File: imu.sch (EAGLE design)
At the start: 51 parts, among them IC1 TM4C123[6,F]XXPM, IC2 FT230XQ, U1 MPU-6000QFN-24, U2 ADXL345

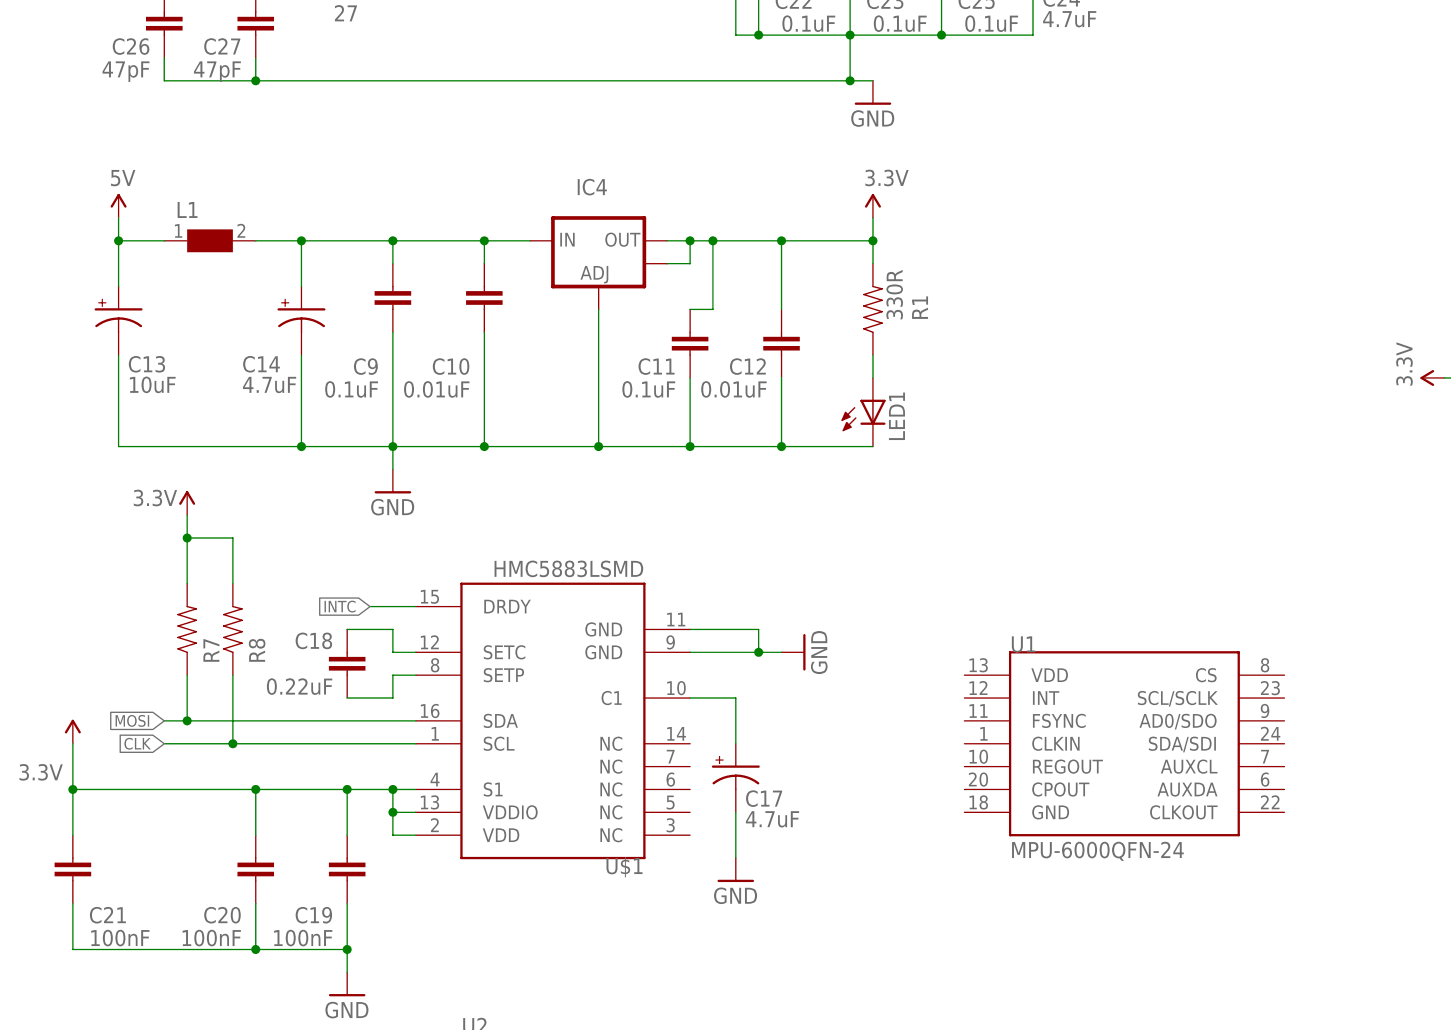
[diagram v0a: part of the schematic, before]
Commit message: Modification to schematics and board
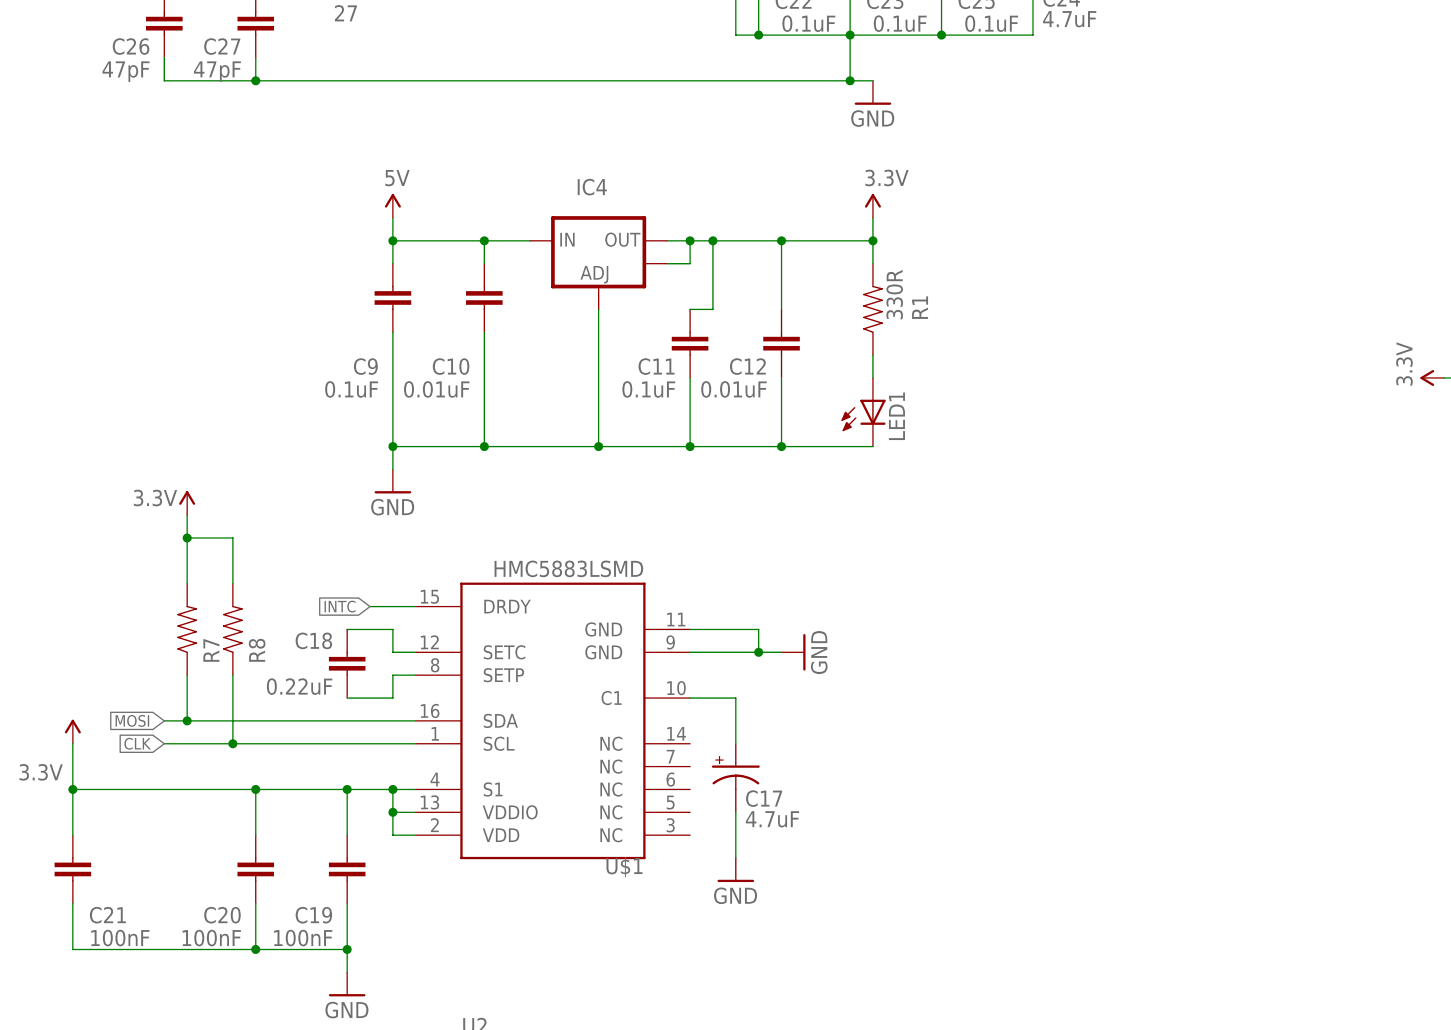
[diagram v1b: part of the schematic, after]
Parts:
- removed C13: 10uF, SparkFun-Capacitors:CAP_POL1206
- removed C14: 4.7uF, SparkFun-Capacitors:CAP_POL1206
- removed L1: 10uH, Wuerth_Elektronik_eiSos_V6:WE-CBF_1206
- removed U1: MPU-6000QFN-24, SparkFun-Sensors:MPU-6000QFN-24
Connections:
- removed net N$3: C10.2, C14.+, C9.2, IC4.IN, L1.2
- net 5V: now also C10.2, C9.2, IC4.IN; no longer C13.+, L1.1
- net GND: no longer C13.-, C14.-
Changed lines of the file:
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@@
 <part name="C12" library="SparkFun-Passives" deviceset="CAP" device="0603-CAP" value="0.01uF"/>
 <part name="GND9" library="SparkFun-Aesthetics" deviceset="GND" device=""/>
-<part name="L1" library="Wuerth_Elektronik_eiSos_V6" deviceset="WE-CBF" device="_1206" value="10uH"/>
-<part name="C13" library="SparkFun-Capacitors" deviceset="CAP_POL" device="1206" value="10uF"/>
-<part name="C14" library="SparkFun-Capacitors" deviceset="CAP_POL" device="1206" value="4.7uF"/>
 <part name="JP1" library="SparkFun-Connectors" deviceset="USB" device="SMD"/>
 <part name="GND10" library="SparkFun-Aesthetics" deviceset="GND" device=""/>
 <part name="R1" library="SparkFun-Resistors" deviceset="RESISTOR" device="0805-RES" value="330R"/>
 <part name="LED1" library="SparkFun-LED" deviceset="LED" device="0603"/>
-<part name="SUPPLY10" library="SparkFun-Aesthetics" deviceset="5V" device=""/>
 <part name="C17" library="SparkFun-Capacitors" deviceset="CAP_POL" device="1206" value="4.7uF"/>
 <part name="GND12" library="SparkFun-Aesthetics" deviceset="GND" device=""/>
@@
 <part name="GND15" library="SparkFun-Aesthetics" deviceset="GND" device=""/>
 <part name="SUPPLY18" library="SparkFun-Aesthetics" deviceset="3.3V" device=""/>
-<part name="U1" library="SparkFun-Sensors" deviceset="MPU-6000" device="QFN-24"/>
 <part name="SUPPLY4" library="SparkFun-Aesthetics" deviceset="3.3V" device=""/>
 <part name="SUPPLY7" library="SparkFun-Aesthetics" deviceset="3.3V" device=""/>
 <part name="SUPPLY9" library="SparkFun-Aesthetics" deviceset="3.3V" device=""/>
 <part name="U2" library="SparkFun-Sensors" deviceset="ADXL345" device=""/>
+<part name="SUPPLY2" library="SparkFun-Aesthetics" deviceset="5V" device=""/>
 </parts>
 <sheets>
@@
 </instance>
 <instance part="GND9" gate="1" x="-73.66" y="-238.76"/>
-<instance part="L1" gate="G$1" x="-93.98" y="-210.82" smashed="yes">
-<attribute name="NAME" x="-97.79" y="-208.28" size="1.778" layer="95"/>
-</instance>
-<instance part="C13" gate="G$1" x="-104.14" y="-218.44" smashed="yes">
-<attribute name="NAME" x="-103.124" y="-225.425" size="1.778" layer="95"/>
-<attribute name="VALUE" x="-103.124" y="-227.711" size="1.778" layer="96"/>
-</instance>
-<instance part="C14" gate="G$1" x="-83.82" y="-218.44" smashed="yes">
-<attribute name="NAME" x="-90.424" y="-225.425" size="1.778" layer="95"/>
-<attribute name="VALUE" x="-90.424" y="-227.711" size="1.778" layer="96"/>
-</instance>
 <instance part="JP1" gate="G$1" x="-106.68" y="-170.18" rot="R180"/>
 <instance part="GND10" gate="1" x="-99.06" y="-162.56" rot="R180"/>
@@
 <attribute name="VALUE" x="-14.605" y="-233.172" size="1.778" layer="96" rot="R90"/>
 </instance>
-<instance part="SUPPLY10" gate="G$1" x="-104.14" y="-208.28"/>
 <instance part="C17" gate="G$1" x="-35.56" y="-269.24" smashed="yes">
 <attribute name="NAME" x="-34.544" y="-273.685" size="1.778" layer="95"/>
@@
 <instance part="GND15" gate="1" x="48.26" y="-147.32" rot="R90"/>
 <instance part="SUPPLY18" gate="G$1" x="45.72" y="-152.4" rot="R270"/>
-<instance part="U1" gate="G$1" x="7.62" y="-266.7"/>
 <instance part="SUPPLY4" gate="G$1" x="43.18" y="-226.06" rot="R90"/>
 <instance part="SUPPLY7" gate="G$1" x="129.54" y="-220.98"/>
 <instance part="SUPPLY9" gate="G$1" x="-20.32" y="-208.28"/>
 <instance part="U2" gate="G$1" x="-58.42" y="-312.42"/>
+<instance part="SUPPLY2" gate="G$1" x="-73.66" y="-208.28"/>
 </instances>
 <busses>
@@
 <segment>
 <pinref part="C9" gate="G$1" pin="1"/>
-<wire x1="-83.82" y1="-233.68" x2="-73.66" y2="-233.68" width="0.1524" layer="91"/>
 <wire x1="-73.66" y1="-233.68" x2="-73.66" y2="-220.98" width="0.1524" layer="91"/>
 <pinref part="C10" gate="G$1" pin="1"/>
@@
 <pinref part="GND9" gate="1" pin="GND"/>
 <wire x1="-73.66" y1="-236.22" x2="-73.66" y2="-233.68" width="0.1524" layer="91"/>
-<pinref part="C14" gate="G$1" pin="-"/>
-<wire x1="-83.82" y1="-223.52" x2="-83.82" y2="-233.68" width="0.1524" layer="91"/>
-<pinref part="C13" gate="G$1" pin="-"/>
-<wire x1="-104.14" y1="-223.52" x2="-104.14" y2="-233.68" width="0.1524" layer="91"/>
-<wire x1="-104.14" y1="-233.68" x2="-83.82" y2="-233.68" width="0.1524" layer="91"/>
-<junction x="-83.82" y="-233.68"/>
 <pinref part="LED1" gate="G$1" pin="C"/>
 <wire x1="-20.32" y1="-233.68" x2="-30.48" y2="-233.68" width="0.1524" layer="91"/>
@@
 </segment>
 </net>
-<net name="N$3" class="0">
+<net name="5V" class="0">
+<segment>
+<pinref part="JP1" gate="G$1" pin="VBUS"/>
+<wire x1="-104.14" y1="-172.72" x2="-93.98" y2="-172.72" width="0.1524" layer="91"/>
+<wire x1="-93.98" y1="-172.72" x2="-93.98" y2="-165.1" width="0.1524" layer="91"/>
+<pinref part="SUPPLY3" gate="G$1" pin="5V"/>
+</segment>
 <segment>
 <pinref part="IC4" gate="G$1" pin="IN"/>
@@
 <pinref part="C9" gate="G$1" pin="2"/>
 <wire x1="-73.66" y1="-213.36" x2="-73.66" y2="-210.82" width="0.1524" layer="91"/>
+<junction x="-63.5" y="-210.82"/>
+<pinref part="SUPPLY2" gate="G$1" pin="5V"/>
+<wire x1="-73.66" y1="-210.82" x2="-73.66" y2="-208.28" width="0.1524" layer="91"/>
 <junction x="-73.66" y="-210.82"/>
-<junction x="-63.5" y="-210.82"/>
-<pinref part="C14" gate="G$1" pin="+"/>
-<wire x1="-73.66" y1="-210.82" x2="-83.82" y2="-210.82" width="0.1524" layer="91"/>
-<wire x1="-83.82" y1="-210.82" x2="-83.82" y2="-215.9" width="0.1524" layer="91"/>
-<pinref part="L1" gate="G$1" pin="2"/>
-<wire x1="-88.9" y1="-210.82" x2="-83.82" y2="-210.82" width="0.1524" layer="91"/>
-<junction x="-83.82" y="-210.82"/>
 </segment>
 </net>
-<net name="5V" class="0">
-<segment>
-<pinref part="JP1" gate="G$1" pin="VBUS"/>
-<wire x1="-104.14" y1="-172.72" x2="-93.98" y2="-172.72" width="0.1524" layer="91"/>
-<wire x1="-93.98" y1="-172.72" x2="-93.98" y2="-165.1" width="0.1524" layer="91"/>
-<pinref part="SUPPLY3" gate="G$1" pin="5V"/>
-</segment>
-<segment>
-<pinref part="L1" gate="G$1" pin="1"/>
-<pinref part="C13" gate="G$1" pin="+"/>
-<wire x1="-99.06" y1="-210.82" x2="-104.14" y2="-210.82" width="0.1524" layer="91"/>
-<wire x1="-104.14" y1="-210.82" x2="-104.14" y2="-215.9" width="0.1524" layer="91"/>
-<pinref part="SUPPLY10" gate="G$1" pin="5V"/>
-<wire x1="-104.14" y1="-210.82" x2="-104.14" y2="-208.28" width="0.1524" layer="91"/>
-<junction x="-104.14" y="-210.82"/>
-</segment>
-</net>
